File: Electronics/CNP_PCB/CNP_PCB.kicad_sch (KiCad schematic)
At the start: 0 parts

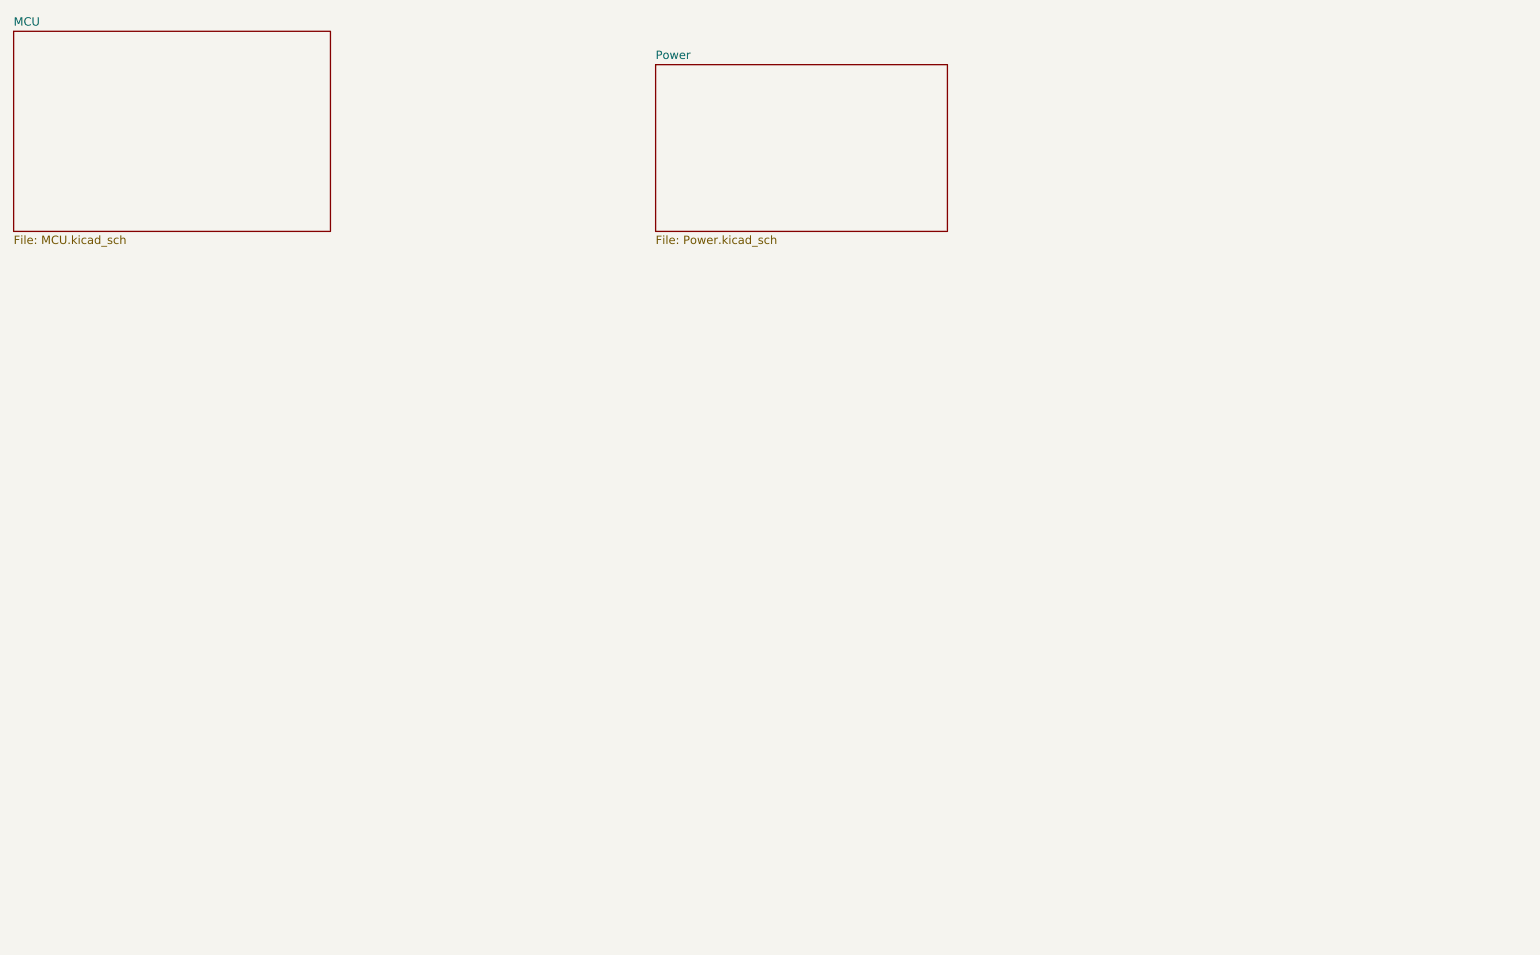
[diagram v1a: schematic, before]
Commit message: added switch logic for emulating buttons
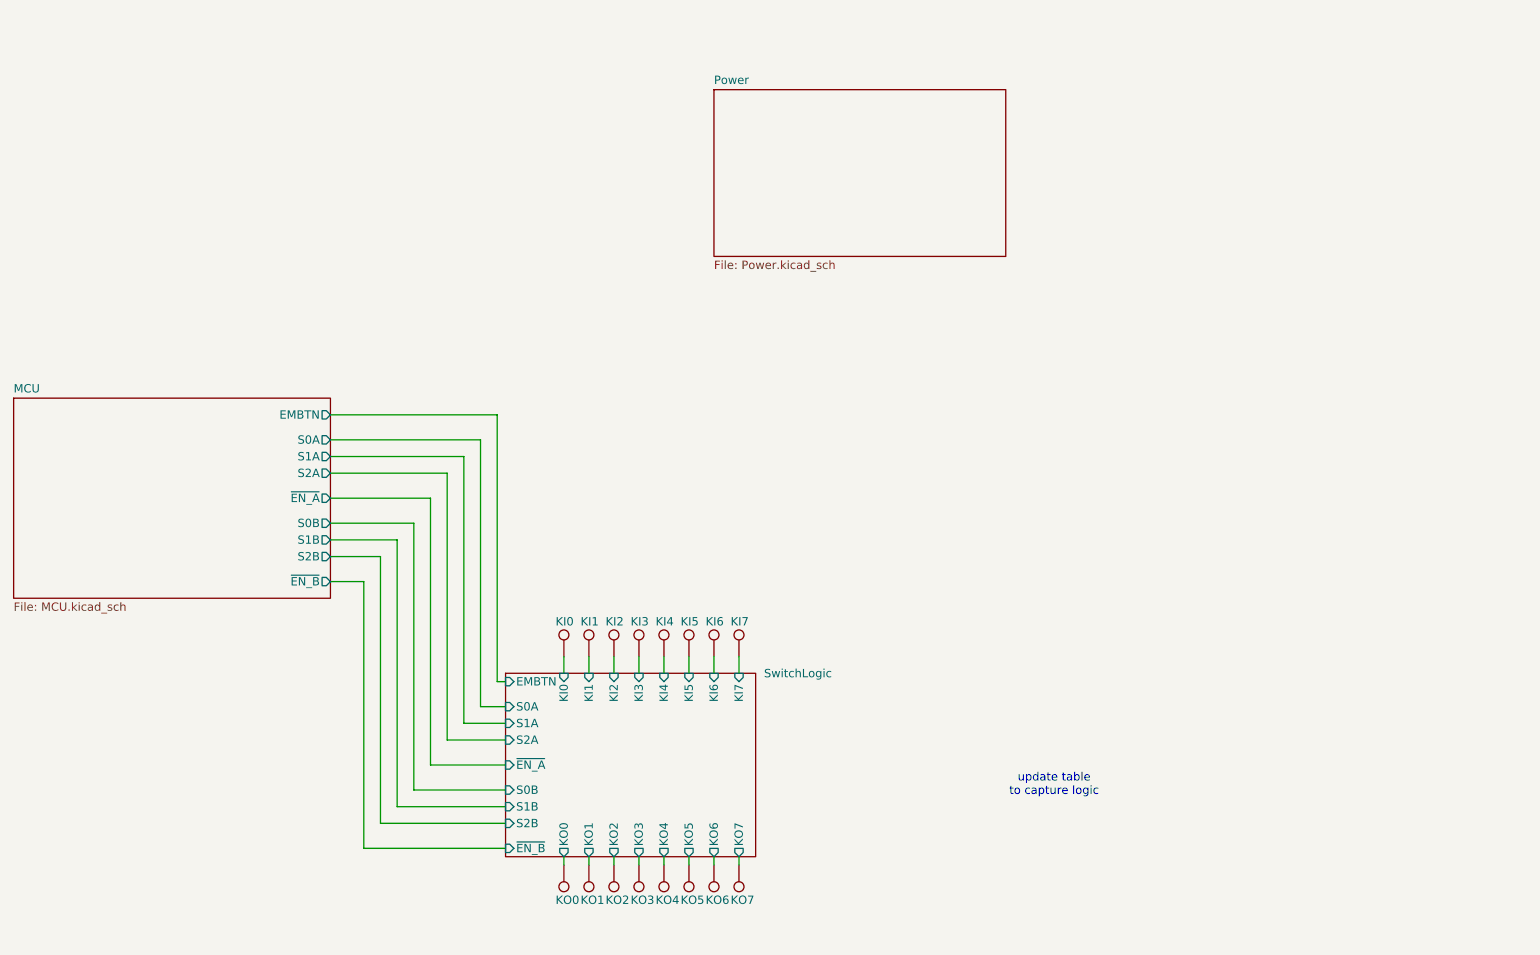
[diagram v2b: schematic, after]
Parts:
- added TP1: KI0, TestPoint:TestPoint_Pad_D2.0mm, symbol Connector:TestPoint
- added TP10: KO1, TestPoint:TestPoint_Pad_D2.0mm, symbol Connector:TestPoint
- added TP11: KO2, TestPoint:TestPoint_Pad_D2.0mm, symbol Connector:TestPoint
- added TP12: KO3, TestPoint:TestPoint_Pad_D2.0mm, symbol Connector:TestPoint
- added TP13: KO4, TestPoint:TestPoint_Pad_D2.0mm, symbol Connector:TestPoint
- added TP14: KO5, TestPoint:TestPoint_Pad_D2.0mm, symbol Connector:TestPoint
- added TP15: KO6, TestPoint:TestPoint_Pad_D2.0mm, symbol Connector:TestPoint
- added TP16: KO7, TestPoint:TestPoint_Pad_D2.0mm, symbol Connector:TestPoint
- added TP2: KI1, TestPoint:TestPoint_Pad_D2.0mm, symbol Connector:TestPoint
- added TP3: KI2, TestPoint:TestPoint_Pad_D2.0mm, symbol Connector:TestPoint
- added TP4: KI3, TestPoint:TestPoint_Pad_D2.0mm, symbol Connector:TestPoint
- added TP5: KI4, TestPoint:TestPoint_Pad_D2.0mm, symbol Connector:TestPoint
- added TP6: KI5, TestPoint:TestPoint_Pad_D2.0mm, symbol Connector:TestPoint
- added TP7: KI6, TestPoint:TestPoint_Pad_D2.0mm, symbol Connector:TestPoint
- added TP8: KI7, TestPoint:TestPoint_Pad_D2.0mm, symbol Connector:TestPoint
- added TP9: KO0, TestPoint:TestPoint_Pad_D2.0mm, symbol Connector:TestPoint
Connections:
- new net SwitchLogic/KI0: TP1.1
- new net SwitchLogic/KI1: TP2.1
- new net SwitchLogic/KI2: TP3.1
- new net SwitchLogic/KI3: TP4.1
- new net SwitchLogic/KI4: TP5.1
- new net SwitchLogic/KI5: TP6.1
- new net SwitchLogic/KI6: TP7.1
- new net SwitchLogic/KI7: TP8.1
- new net SwitchLogic/KO0: TP9.1
- new net SwitchLogic/KO1: TP10.1
- new net SwitchLogic/KO2: TP11.1
- new net SwitchLogic/KO3: TP12.1
- new net SwitchLogic/KO4: TP13.1
- new net SwitchLogic/KO5: TP14.1
- new net SwitchLogic/KO6: TP15.1
- new net SwitchLogic/KO7: TP16.1
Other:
- added sheet SwitchLogic (SwitchLogic.kicad_sch)
- sheet MCU ports: added EMBTN, S0A, S0B, S1A, S1B, S2A, S2B, ~{EN_A}, ~{EN_B}; removed none
- note added: "update table to capture logic"

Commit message: changes made to button read logic
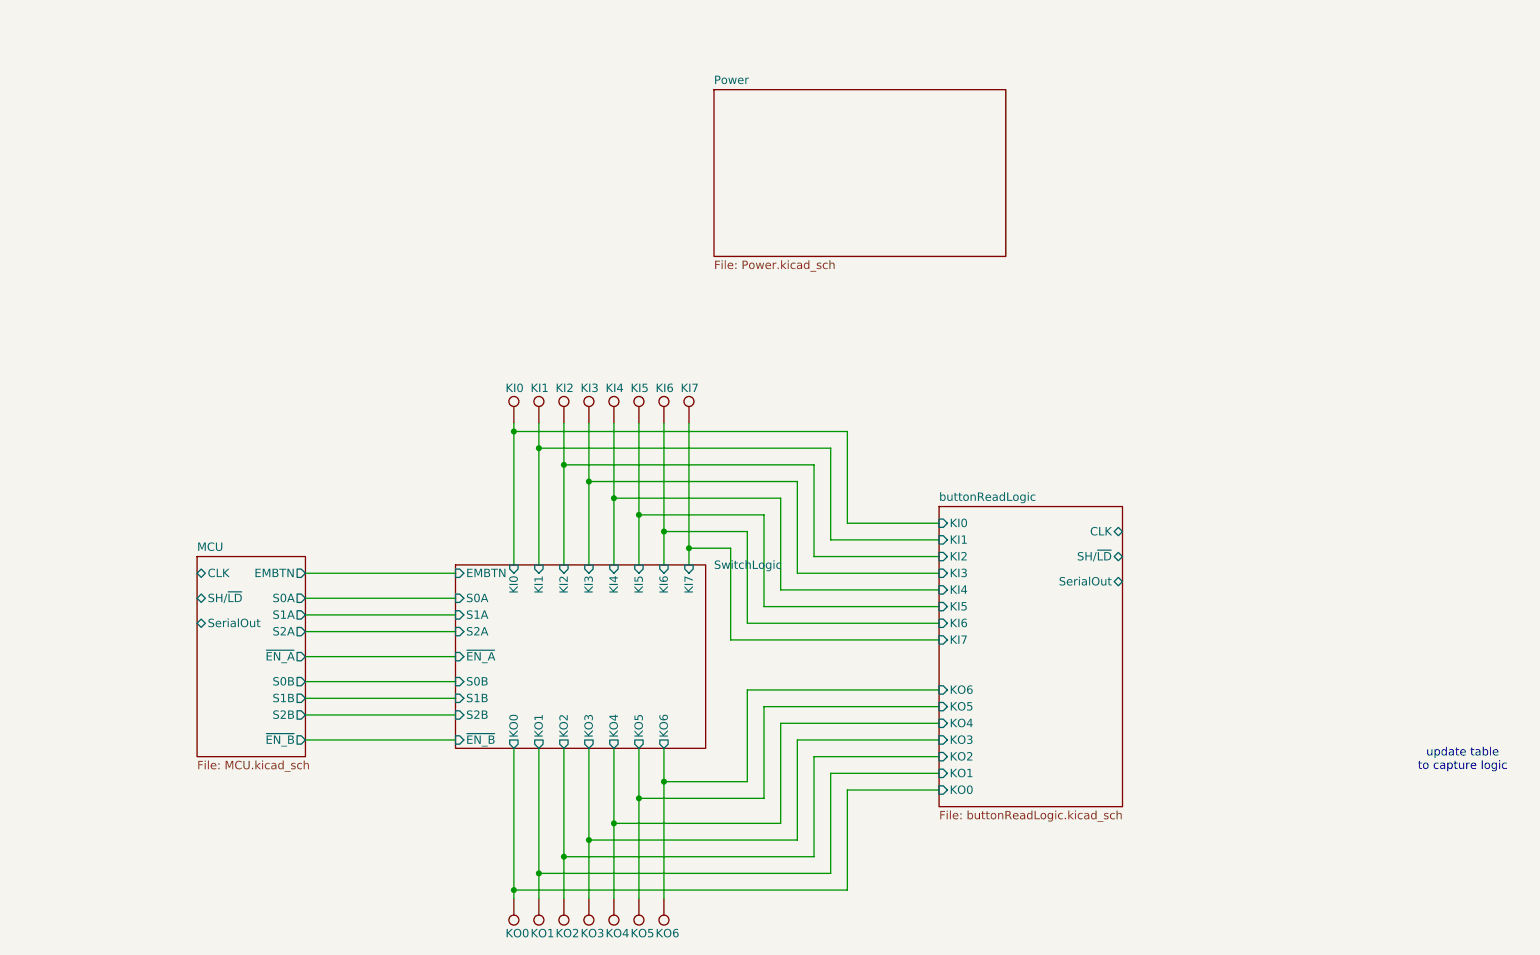
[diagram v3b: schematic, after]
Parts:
- removed TP16: KO7, TestPoint:TestPoint_Pad_D2.0mm, symbol Connector:TestPoint
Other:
- added sheet buttonReadLogic (buttonReadLogic.kicad_sch)
- sheet MCU ports: added CLK, SH/~{LD}, SerialOut; removed none
- sheet SwitchLogic ports: added none; removed KO7
